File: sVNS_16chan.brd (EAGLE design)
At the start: 54.6 x 25.1 mm, 55 parts, among them IC1 EFM8SB10F8G-A-CSP16R, IC2 OPA990IDCKR, J1 TSM-130-01-F-SV, U1 NT3H2211W0FHKH, U2 LT8410EDC-1#TRMPBF, U3 MUX36S16IRSNR, U4 MUX36S16IRSNR

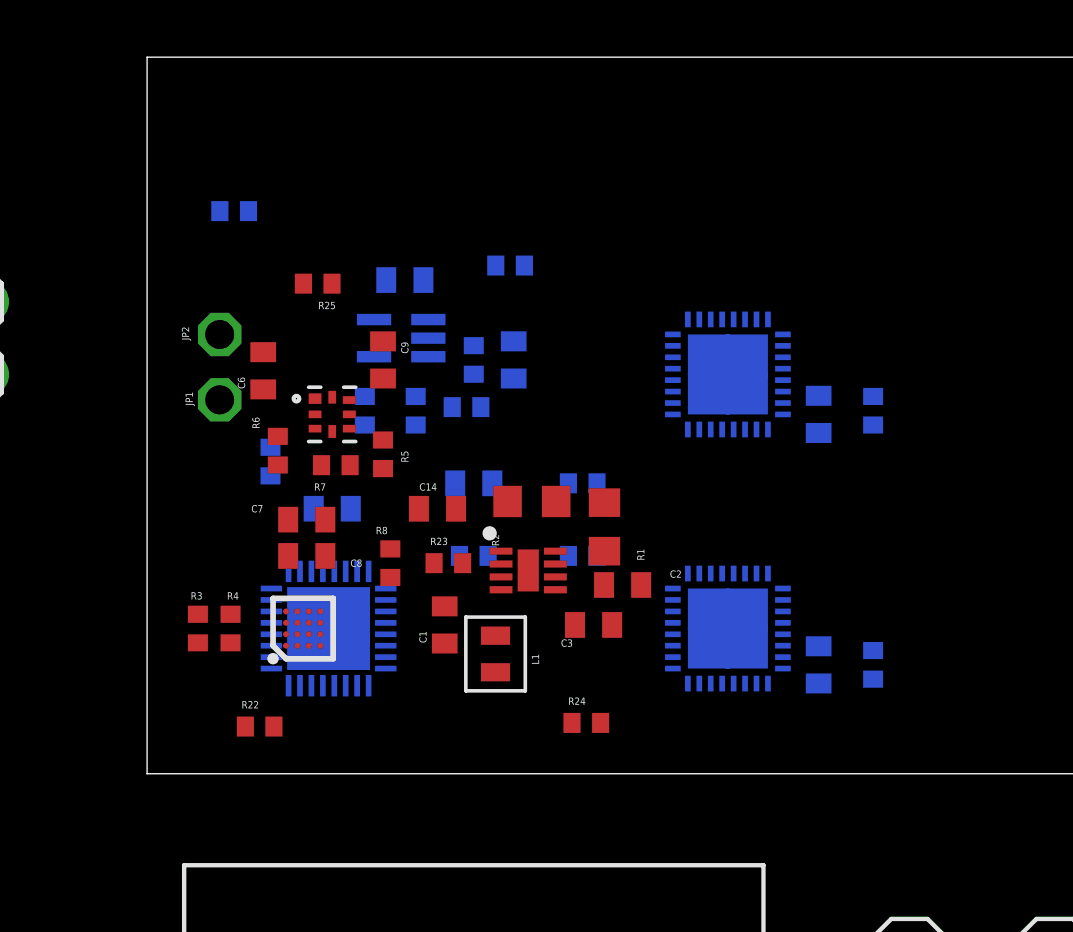
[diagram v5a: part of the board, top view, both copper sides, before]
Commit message: LT8410 and H-bridge relocated
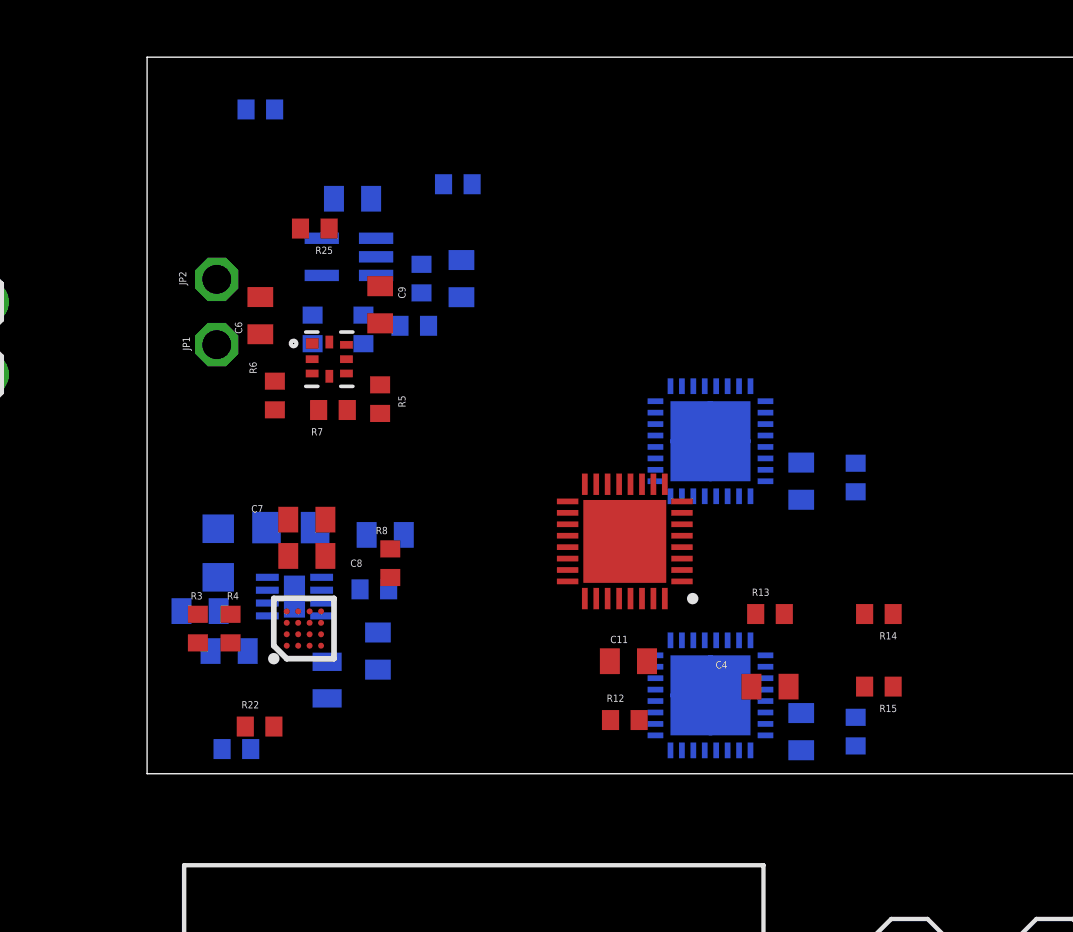
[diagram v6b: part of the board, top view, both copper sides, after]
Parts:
- moved R12 15.3 mm to (16.7, 1.88), flipped to the top, turned to 0 degrees
- moved C2 14.8 mm to (1.85, 5.69), flipped to the bottom
- moved R1 13.5 mm to (2.49, 7.72), flipped to the bottom
- moved C3 12.8 mm to (2.87, 4.29), flipped to the bottom
- moved R15 12.6 mm to (25.6, 3.05), flipped to the top, turned to 180 degrees
- moved C4 12.6 mm to (21.8, 3.05), flipped to the top, turned to 0 degrees
- moved R24 12.3 mm to (3.12, 0.86), flipped to the bottom
- moved C11 11.7 mm to (16.8, 3.94), flipped to the top, turned to 0 degrees
- moved U$1 10.8 mm to (16.7, 8.13), flipped to the top, turned to 180 degrees
- moved R14 10.6 mm to (25.6, 5.59), flipped to the top, turned to 180 degrees
- moved R13 10.6 mm to (21.8, 5.59), flipped to the top, turned to 0 degrees
- moved R2 8.48 mm to (5.03, 8.61), flipped to the bottom
- moved U2 8.23 mm to (5.16, 6.20), flipped to the bottom
- moved L1 5.96 mm to (6.30, 3.28), flipped to the bottom
- moved R17 3.67 mm to (3.96, 23.2)
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
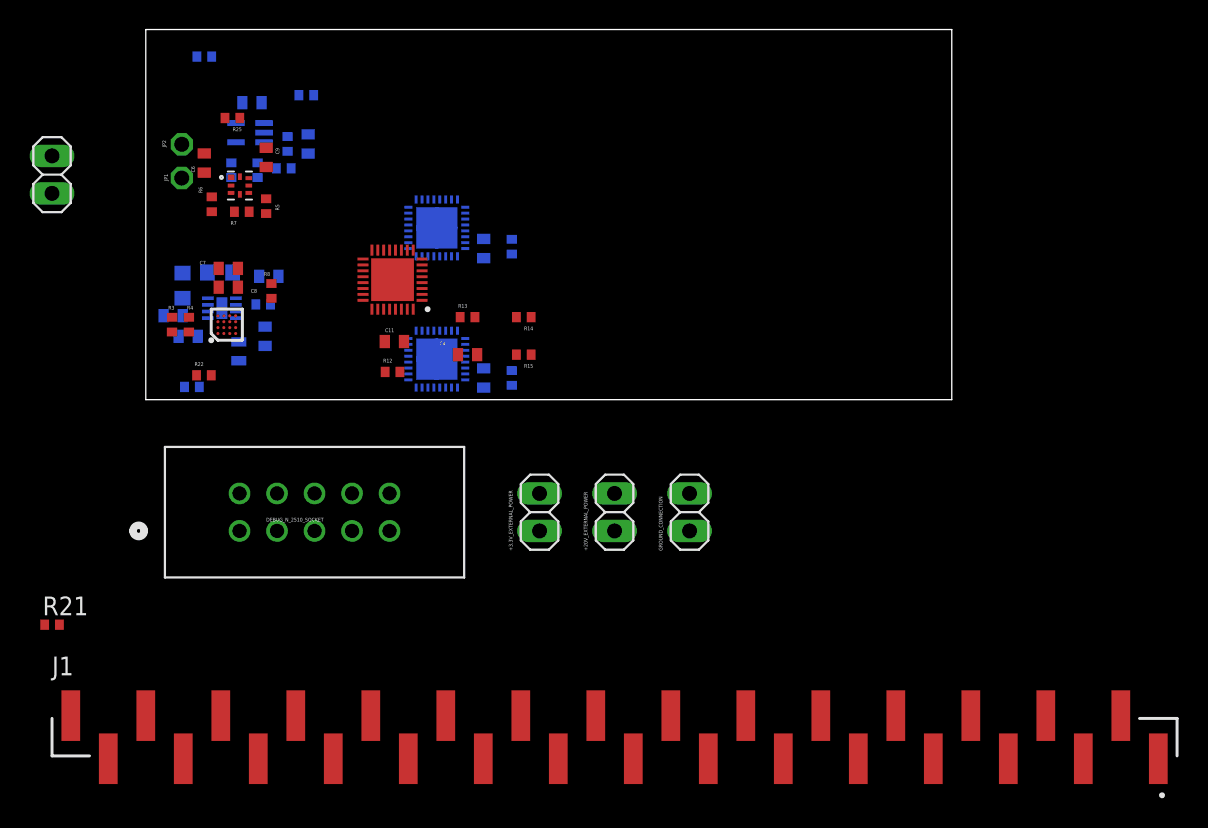
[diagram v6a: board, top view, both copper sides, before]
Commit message: 1) Updated .gitignore as per online recommendations 2)  sch: added third sheet, separated output stage     sch: deleted old pin     sch: added surface mount male connectors and preliminary routed them 3)  brd: draft component location. MUXes and pads on bottom.     Op amp and LT8410 on bottom. H bridge, NT3H and EFM8 on top.     Ready for experiments. GND plane created. No pwr plane yet.
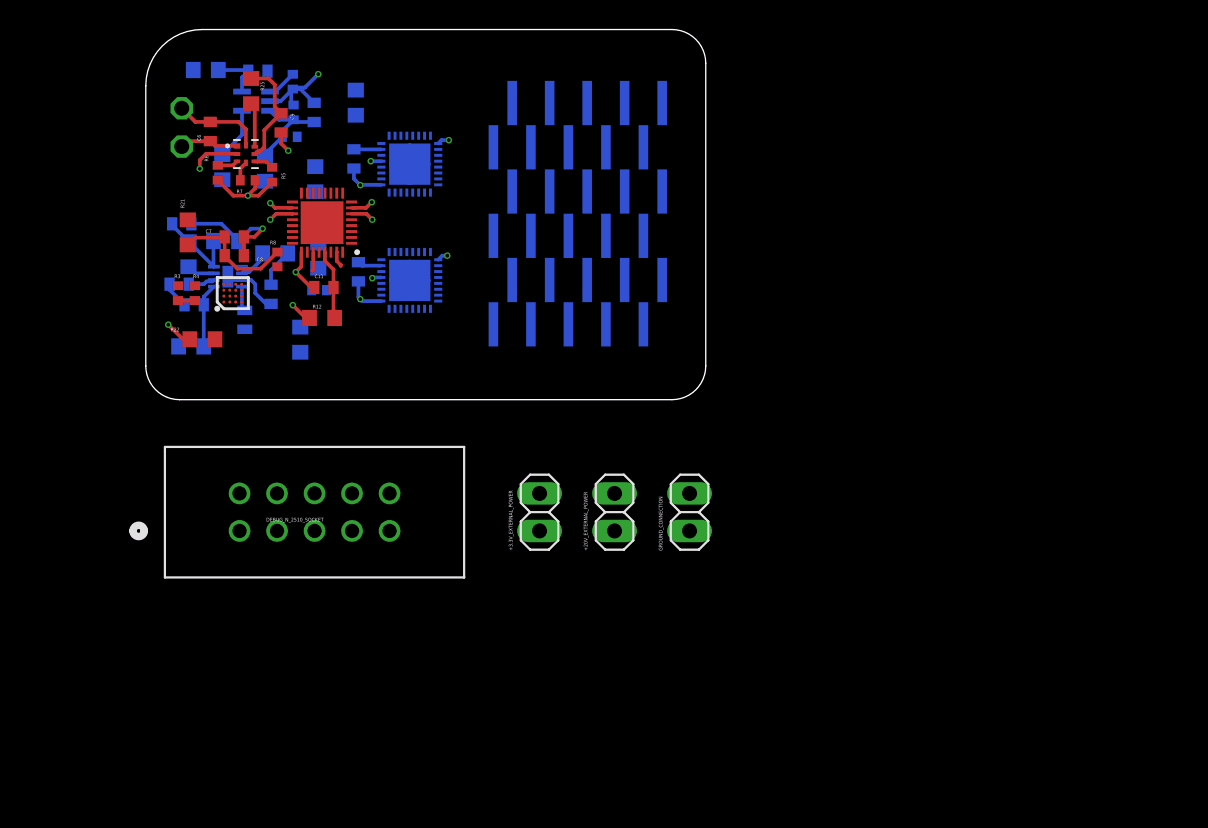
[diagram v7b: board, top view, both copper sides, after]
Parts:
- removed ANTENNA: Antenna connector, pinhead:1X02
- added J2, J3: M50-3631042, M50-3631042:M503631042
- J1: value TSM-130-01-F-SV -> M50-3631042; device TSM-130-01-F-SV:SAMTEC_TSM-130-01-F-SV -> M50-3631042:M503631042
- R12, R14, R15, R16, R17, R18, R19, R20, R21, R22, R23, R24, R25: device sVNS_16chan_lib:R0402 -> sVNS_16chan_lib:R0603
- moved J1 29.6 mm to (29.3, 6.60), flipped to the bottom, turned to 180 degrees
- moved R21 28.1 mm to (2.84, 11.3), turned to 90 degrees
- moved R20 21.4 mm to (14.2, 20.1)
- moved R15 18.5 mm to (11.5, 14.9), flipped to the bottom, turned to 270 degrees
- moved C5 17.2 mm to (14.1, 16.3), turned to 90 degrees
- moved R19 15.6 mm to (10.5, 4.06), turned to 90 degrees
- moved R14 14.5 mm to (11.7, 9.75), flipped to the bottom, turned to 270 degrees
- moved C4 13.7 mm to (11.9, 12.5), flipped to the bottom
- moved U4 13.3 mm to (17.9, 16.0), turned to 270 degrees
- moved R13 10.2 mm to (11.7, 7.42), flipped to the bottom
- moved C10 8.63 mm to (14.4, 8.66), turned to 270 degrees
- moved C14 6.88 mm to (2.44, 11.9)
- moved U$1 6.14 mm to (11.9, 12.0)
- moved C11 6.02 mm to (12.1, 7.59)
- moved R12 6.02 mm to (11.9, 5.54)
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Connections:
- net S10A: now also J1.10
- net S10B: now also J3.10
- net S11A: now also J2.1
- net S11B: now also J2.5
- net S12A: now also J2.2
- net S12B: now also J2.6
- net S13A: now also J2.3
- net S13B: now also J2.7
- net S14A: now also J2.4
- net S14B: now also J2.8
- net S1A: now also J1.1
- net S1B: now also J3.1
- net S2A: now also J1.2
- net S2B: now also J3.2
- net S3A: now also J1.3
- net S3B: now also J3.3
- net S4A: now also J1.4
- net S4B: now also J3.4
- net S5A: now also J1.5
- net S5B: now also J3.5
- net S6A: now also J1.6
- net S6B: now also J3.6
- net S7A: now also J1.7
- net S7B: now also J3.7
- net S8A: now also J1.8
- net S8B: now also J3.8
- net S9A: now also J1.9
- net S9B: now also J3.9
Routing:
- net GND: track 0.00 -> 36.3 mm, vias 0 -> 9
- net +3.3V: track 0.00 -> 15.4 mm, vias 0 -> 1
- net +3.3V_VDD: track 0.00 -> 8.39 mm
- net I_OUT-_PIN: track 0.00 -> 6.56 mm
- net LB: track 0.00 -> 6.01 mm
- net FBP: track 0.00 -> 5.84 mm
- net MUX36D08_+20V: track 0.00 -> 4.70 mm
- net +20V_PIN: track 0.00 -> 4.33 mm
- net LA: track 0.00 -> 4.03 mm
- net P0.7_IREF: track 0.00 -> 3.90 mm, vias 0 -> 1
- net OPAMP_+20V: track 0.00 -> 3.62 mm
- net I_OUT+_PIN: track 0.00 -> 3.52 mm
- net I_OUT+: track 0.00 -> 3.21 mm, vias 0 -> 2
- net I_OUT-: track 0.00 -> 3.20 mm, vias 0 -> 2
- net +3.3V_PIN: track 0.00 -> 3.02 mm
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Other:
- board size 54.6 x 25.1 mm -> 37.9 x 25.1 mm

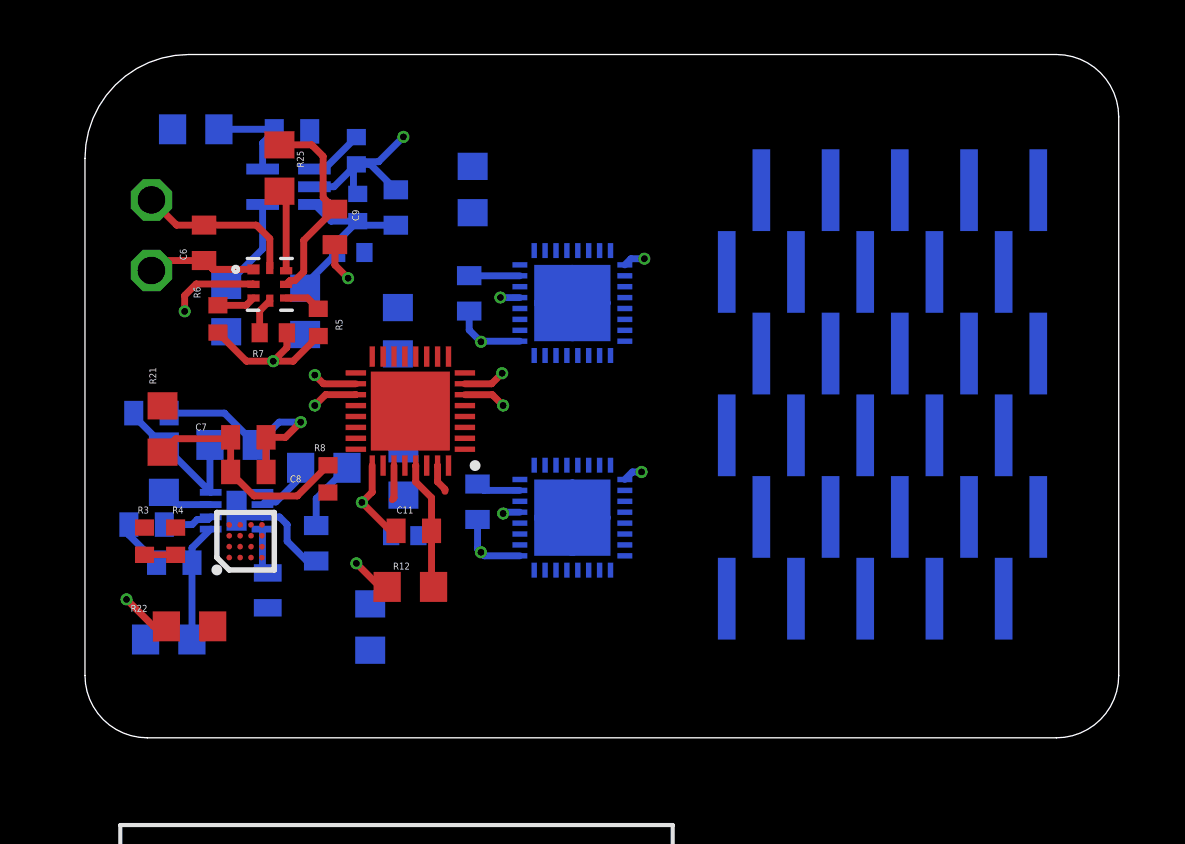
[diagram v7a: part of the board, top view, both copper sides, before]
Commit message: LT8410 and op amp swapped. Optimised layout. Output pins moved to the top layer. Ready for MCU package change.
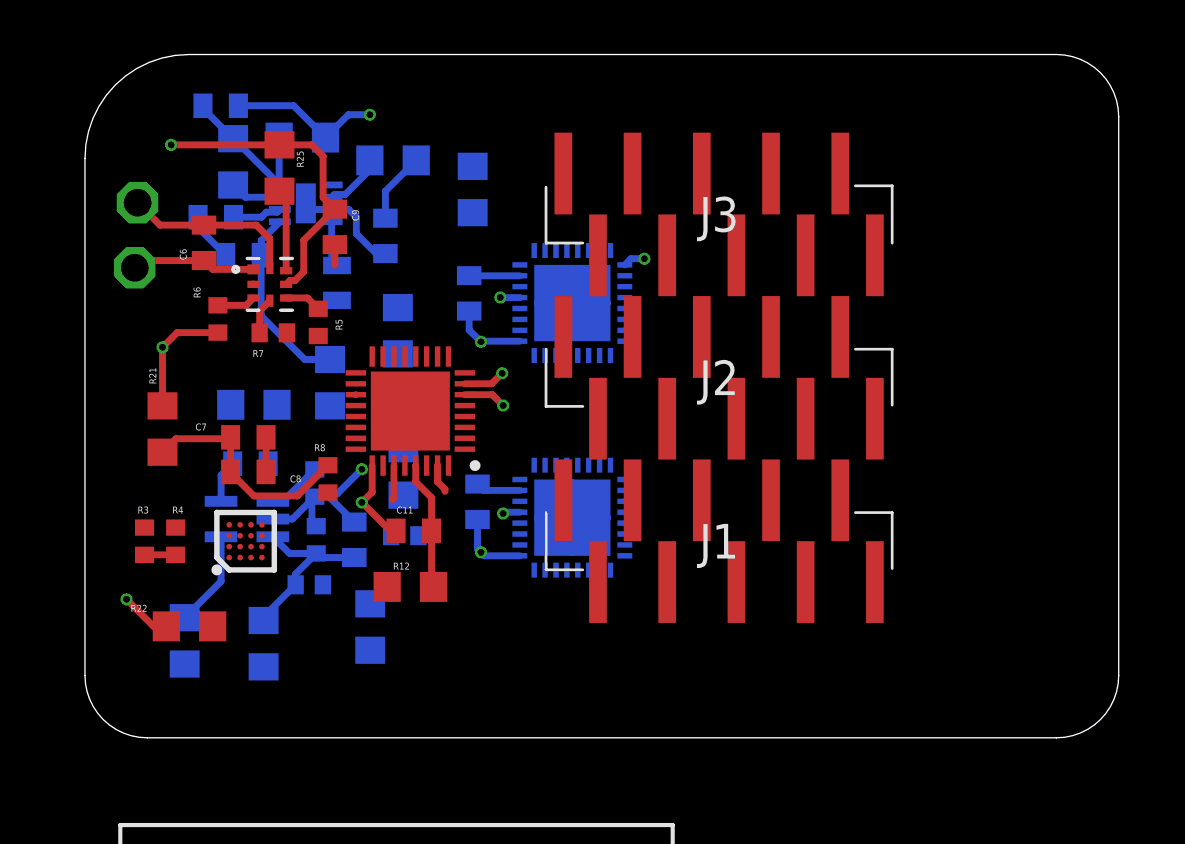
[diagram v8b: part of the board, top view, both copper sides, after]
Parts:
- moved R16 12.3 mm to (3.66, 3.56)
- moved R18 12.3 mm to (6.55, 3.45)
- moved R9 12.3 mm to (8.43, 9.35)
- moved C12 12.3 mm to (6.07, 10.1)
- moved C13 12.3 mm to (9.88, 7.26)
- moved IC2 12.3 mm to (5.94, 8.03)
- moved R10 12.3 mm to (8.23, 5.61)
- moved R11 12.3 mm to (8.48, 7.26)
- moved C14 11.6 mm to (4.98, 23.2)
- moved C3 11.6 mm to (5.82, 17.7)
- moved C1 11.6 mm to (11.0, 18.4)
- moved C2 11.6 mm to (4.80, 19.1)
- moved L1 11.6 mm to (9.25, 16.7)
- moved R1 11.6 mm to (5.44, 21.1)
- moved R2 11.6 mm to (7.98, 22.0)
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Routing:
- net GND: track 36.3 -> 30.1 mm, vias 9 -> 6
- net +20V_PIN: track 4.33 -> 7.03 mm
- net +3.3V: track 15.4 -> 18.1 mm, vias 1 -> 2
- net OPAMP_+20V: track 3.62 -> 1.56 mm
- net I_OUT-: track 3.20 -> 1.53 mm, vias 2 -> 1
- net I_OUT+: track 3.21 -> 1.57 mm, vias 2 -> 1
- net +20V: track 1.49 -> 0.27 mm, vias 1 -> 0
- net LA: track 4.03 -> 4.60 mm
